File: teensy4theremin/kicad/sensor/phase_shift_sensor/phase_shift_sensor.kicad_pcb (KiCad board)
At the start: 2 copper layers, 59.7 x 22.9 mm, 14 parts, among them J1 SENSOR, J2 L_IN, J3 L_OUT, J4 ANTENNA, U1 74HC86, U2 sp721

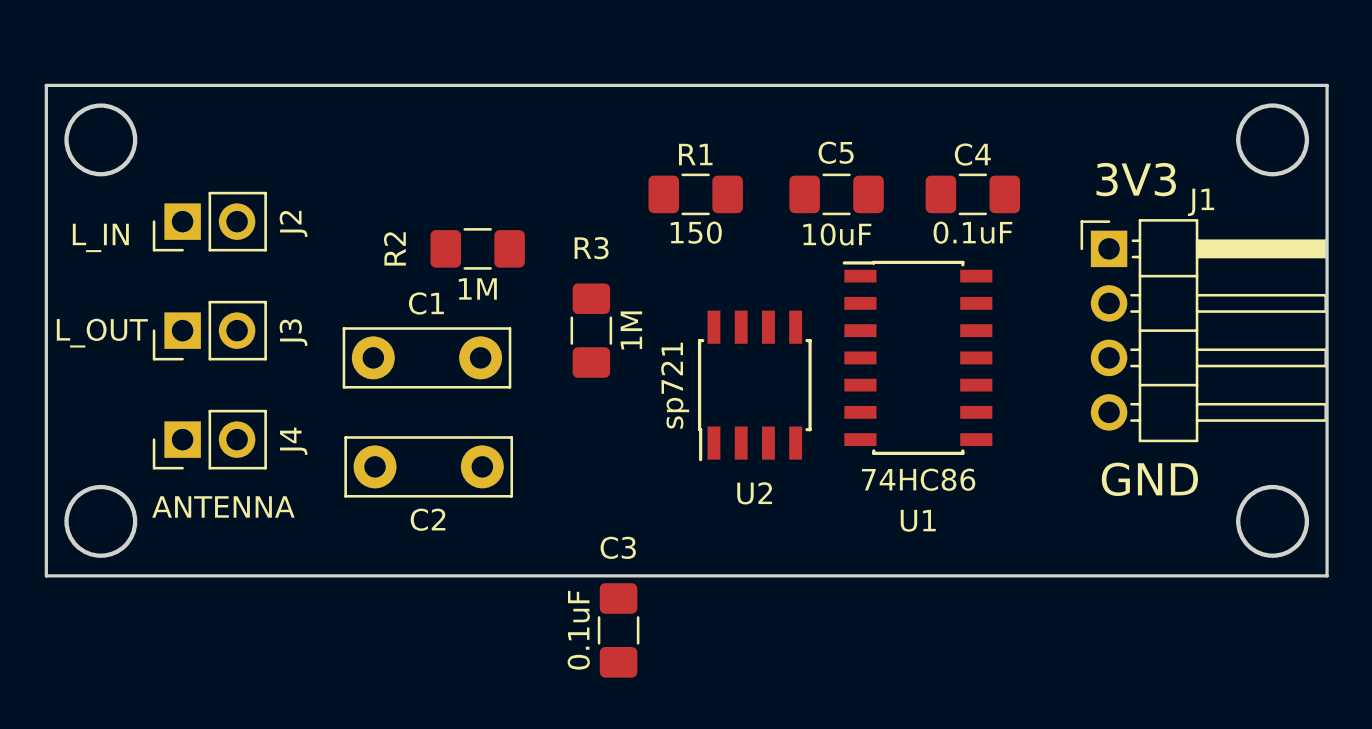
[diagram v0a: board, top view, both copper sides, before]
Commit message: sensor schematic update
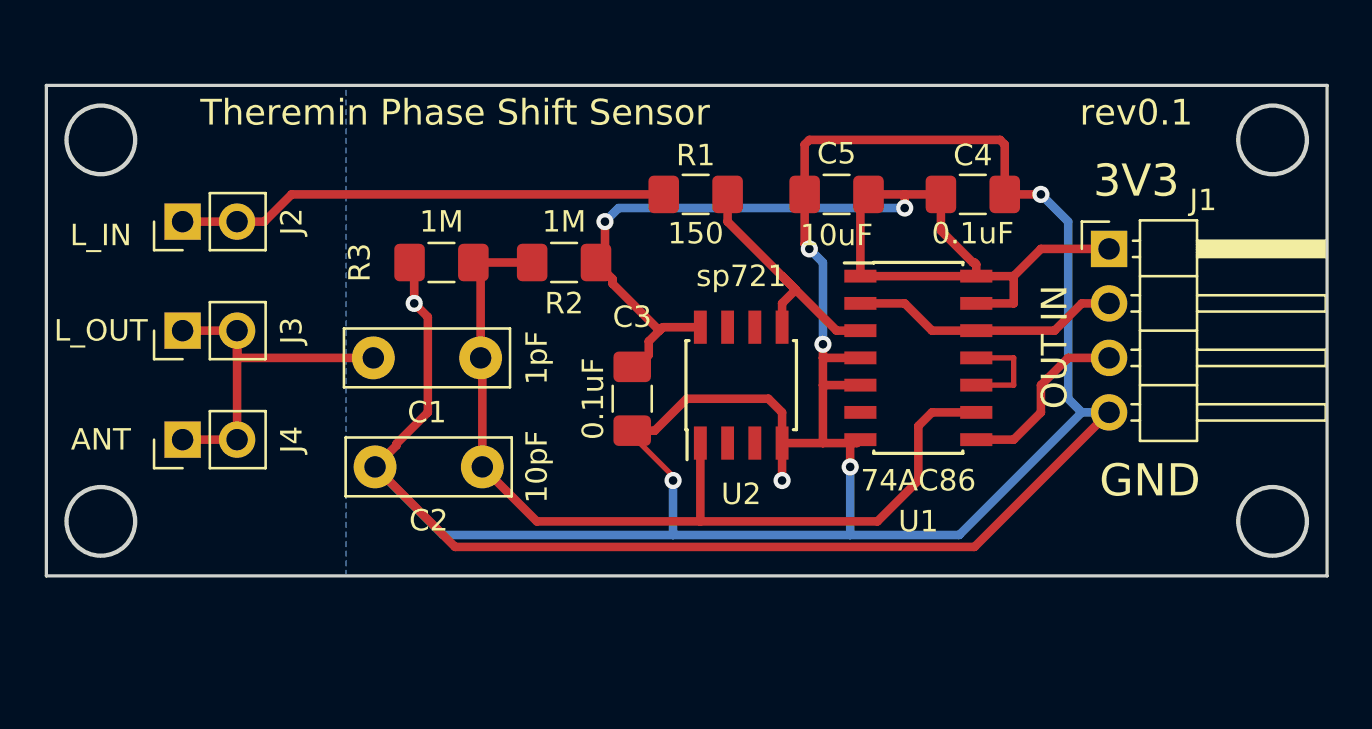
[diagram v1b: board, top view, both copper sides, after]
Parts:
- J4: value ANTENNA -> ANT
- U1: value 74HC86 -> 74AC86
- moved C3 10.8 mm to (117.5, 85.7)
- moved R3 7.67 mm to (108.6, 79.4), turned to 0 degrees
- moved R2 4.08 mm to (114.3, 79.4), turned to 0 degrees
- moved U2 0.63 mm to (122.6, 85.1)
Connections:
- U2 pad 5: Net-(U2-Pad5) -> Net-(R1-Pad2)
- U2 pad 7: Net-(J2-Pad1) -> Net-(U2-Pad7)
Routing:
- net GND: track 0.00 -> 154.5 mm, vias 0 -> 7
- net +3V3: track 0.00 -> 52.8 mm, vias 0 -> 2
- net Net-(C1-Pad2): track 0.00 -> 43.8 mm
- net Net-(J2-Pad1): track 0.00 -> 23.0 mm
- net Net-(C1-Pad1): track 0.00 -> 17.8 mm
- net /REF_CLK: track 0.00 -> 12.6 mm
- net Net-(R1-Pad2): track 0.00 -> 12.5 mm
- net /PWM_OUT: track 0.00 -> 8.51 mm
- net Net-(U1-Pad10): track 0.00 -> 4.76 mm
- added copper zone on B.Cu, net GND
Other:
- board text added: "F_IN"
- board text added: "IN"
- board text added: "OUT"
- board text added: "PWM"
- board text added: "Theremin Phase Shift Sensor"
- board text added: "rev0.1"

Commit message: update
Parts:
- added R4: 470K, Resistor_SMD:R_1206_3216Metric_Pad1.42x1.75mm_HandSolder, F.Cu at (106.7, 79.4)
- C2: value 10pF -> 33pF
- R2, R3: value 1M -> 470K
- moved R2 18.4 mm to (101.0, 92.1), turned to 180 degrees
- moved R3 5.08 mm to (113.7, 79.4)
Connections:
- R2 pad 1: Net-(C1-Pad2) -> GND
- R2 pad 2: +3V3 -> Net-(C1-Pad1)
- R3 pad 1: GND -> Net-(C1-Pad2)
- R3 pad 2: Net-(C1-Pad2) -> +3V3
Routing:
- net GND: track 154.5 -> 161.4 mm
- net Net-(C1-Pad1): track 17.8 -> 22.4 mm
- net +3V3: track 52.8 -> 55.4 mm
- net Net-(C1-Pad2): track 43.8 -> 44.9 mm

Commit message: update
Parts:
- moved J2 42.8 mm to (139.1, 72.4)
- moved J3 14.4 mm to (106.7, 72.4)
- moved J4 8.54 mm to (102.2, 81.3), turned to 180 degrees
- moved R2 6.54 mm to (104.1, 86.4), turned to 90 degrees
- moved R3 3.81 mm to (117.5, 79.4)
- moved R4 3.81 mm to (110.5, 79.4)
- moved C2 2.29 mm to (112.4, 90.2)
- moved C1 1.91 mm to (107.3, 83.8)
- moved R1 1.62 mm to (121.9, 75.6), turned to 270 degrees
- moved C3 1.42 mm to (118.1, 84.5)
- moved J1 0.63 mm to (139.1, 78.7)
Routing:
- net GND: track 161.4 -> 136.1 mm, vias 7 -> 6
- net Net-(C1-Pad1): track 22.4 -> 26.7 mm
- net Net-(C1-Pad2): track 44.9 -> 41.3 mm
- net +3V3: track 55.4 -> 52.0 mm
- net Net-(J2-Pad1): track 23.0 -> 21.0 mm
- net /PWM_OUT: track 8.51 -> 7.13 mm
- net /REF_CLK: track 12.6 -> 12.0 mm
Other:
- board size 59.7 x 22.9 mm -> 51.4 x 24.8 mm
